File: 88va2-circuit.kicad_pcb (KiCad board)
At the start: 4 copper layers, 380 x 237.5 mm, 52 parts, among them CN2 FDD, CN4 TEXT BUS, CN5 LED, IC1 D65101GD055, IC13 SN74ALS374N, IC20 7407, IC21 uPD4990AC, IC22 DIP-14_W7.62mm, IC65 D65101GD110, IC8 SN74ALS374N, IC9 D65200GD076, X2 32.768K

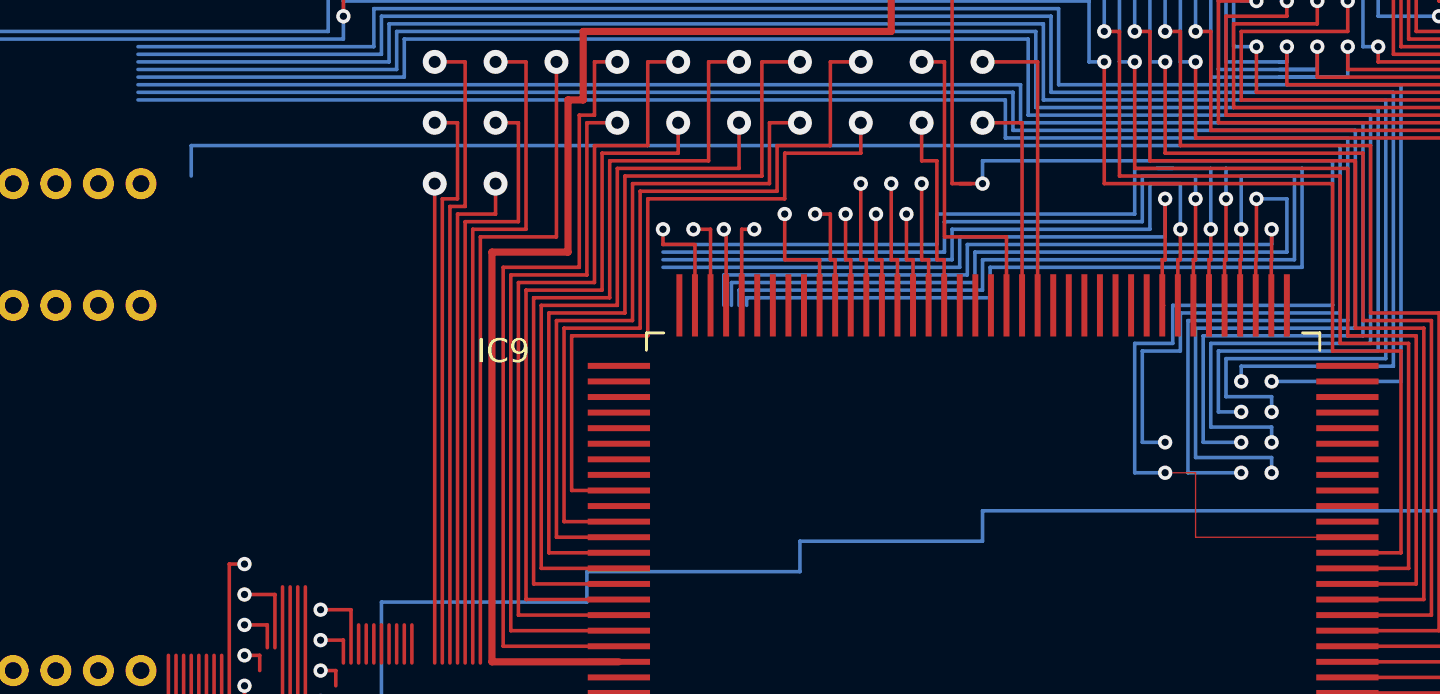
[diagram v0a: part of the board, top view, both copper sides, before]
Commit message: wiring IC9
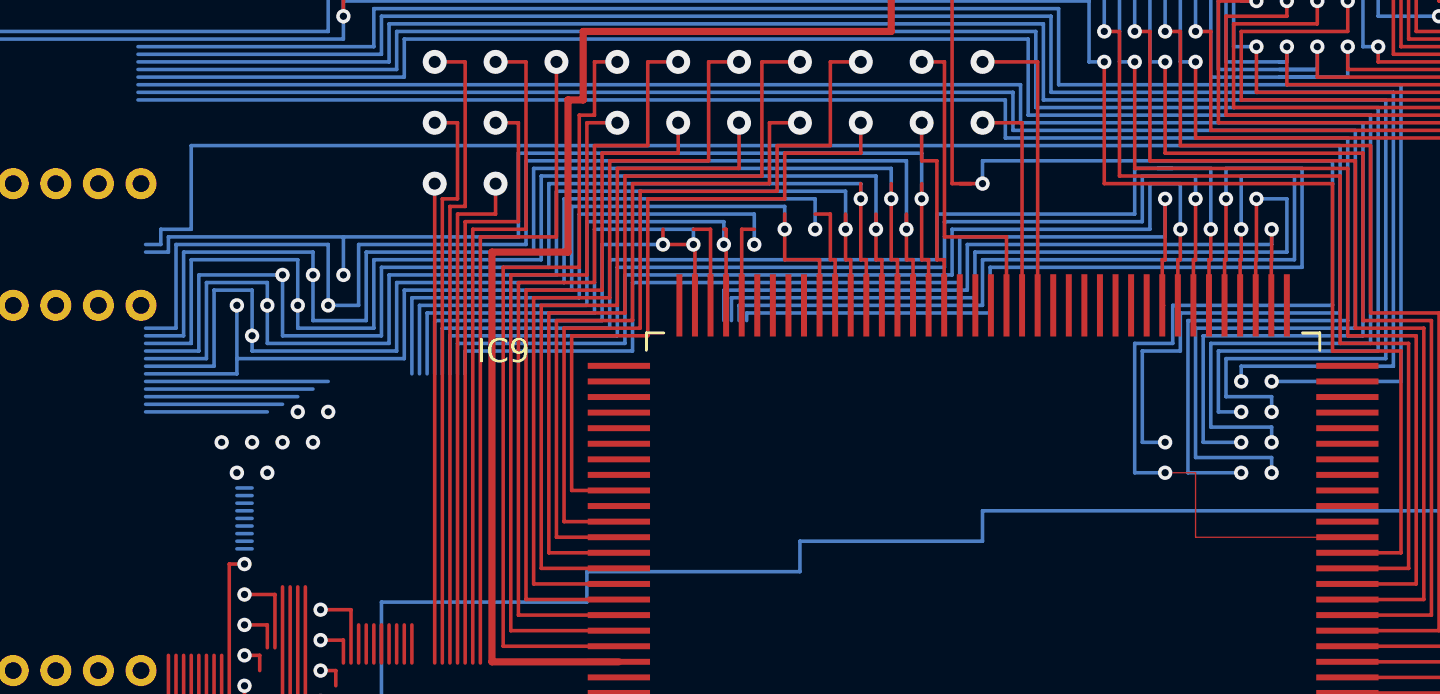
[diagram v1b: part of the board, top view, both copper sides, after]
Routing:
- net (no net): track 4000.6 -> 4515.6 mm, vias 74 -> 90
- net +5V: track 1140.2 -> 1144.0 mm

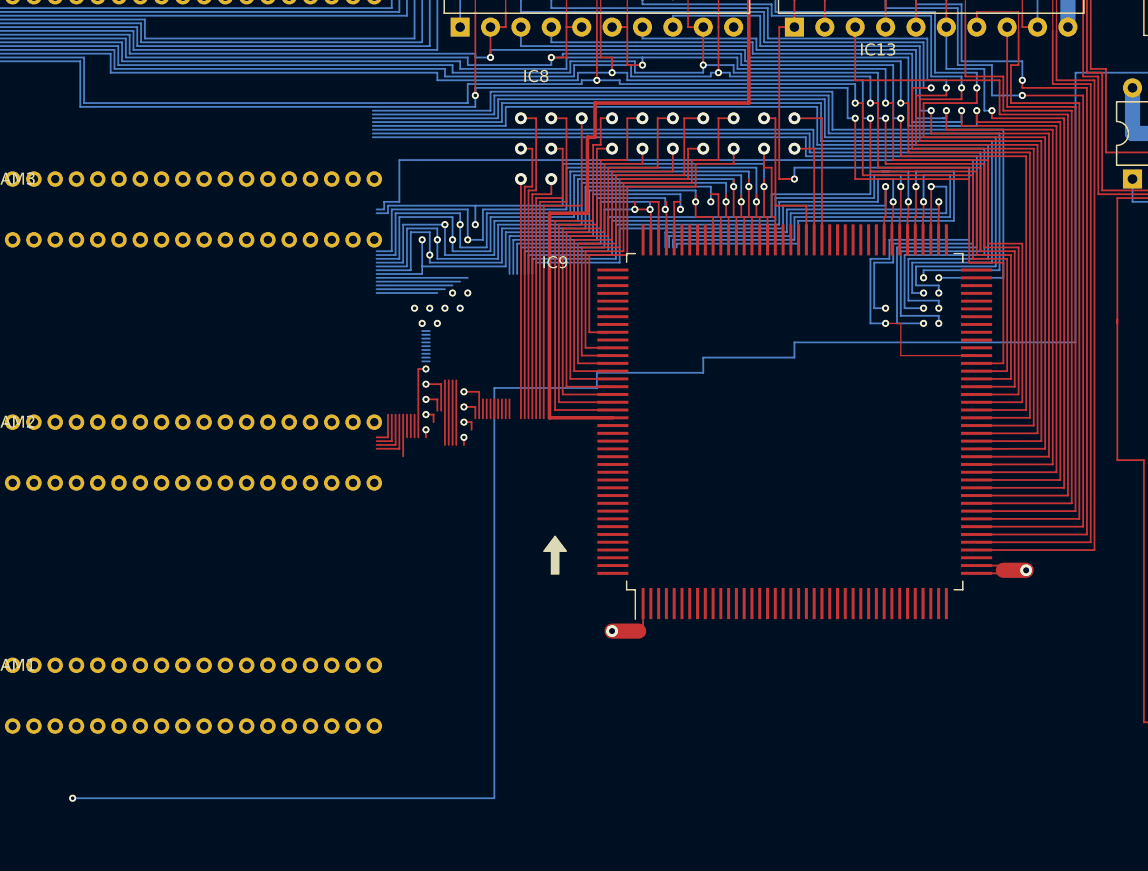
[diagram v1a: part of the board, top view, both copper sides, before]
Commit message: wiring IC9 and GVRAM
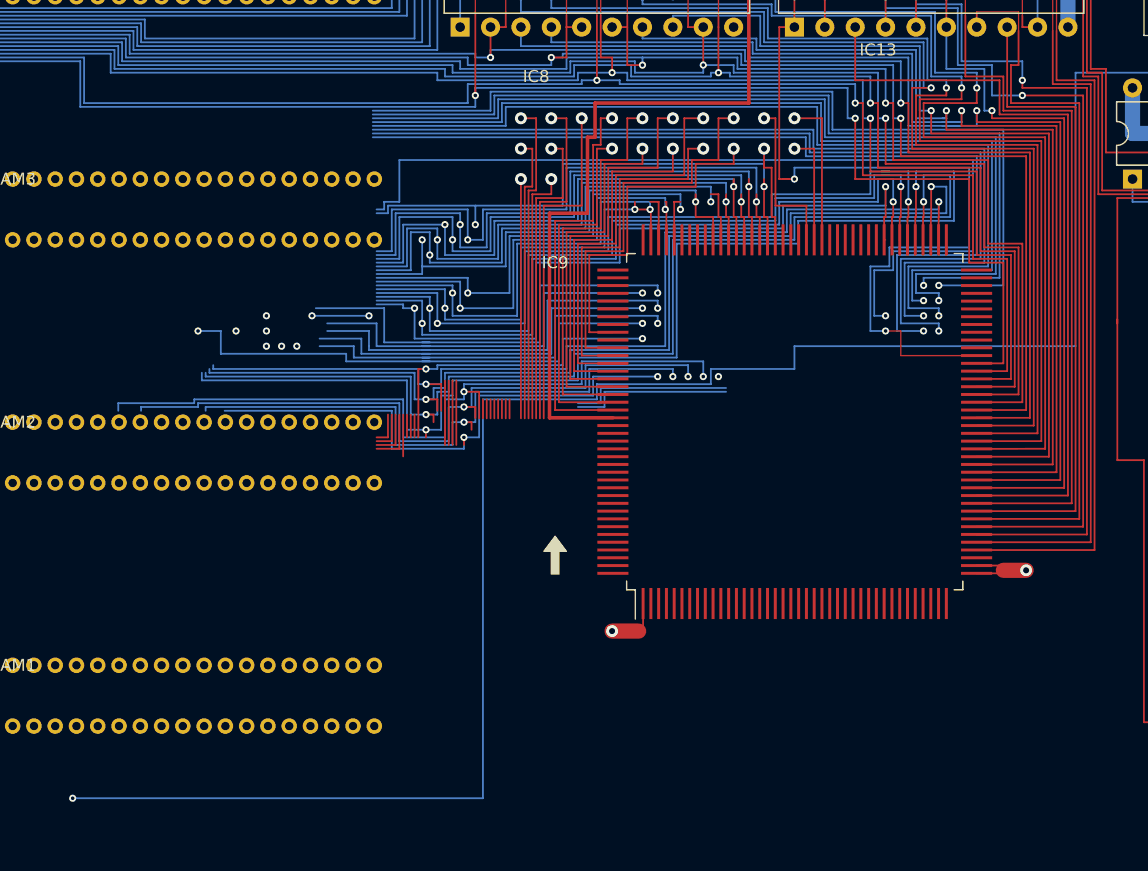
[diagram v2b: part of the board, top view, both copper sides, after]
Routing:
- net (no net): track 4515.6 -> 5333.8 mm, vias 90 -> 111

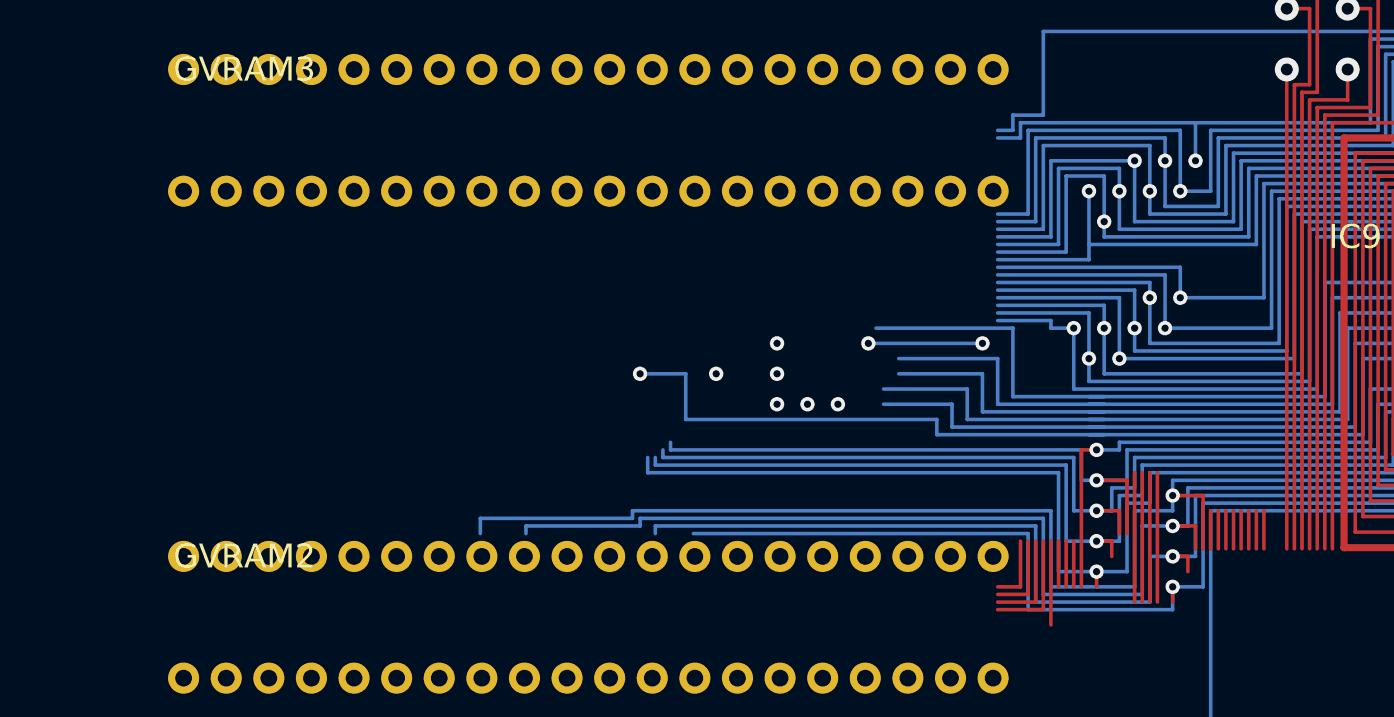
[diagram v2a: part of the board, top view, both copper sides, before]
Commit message: wiring IC9 and GVRAM
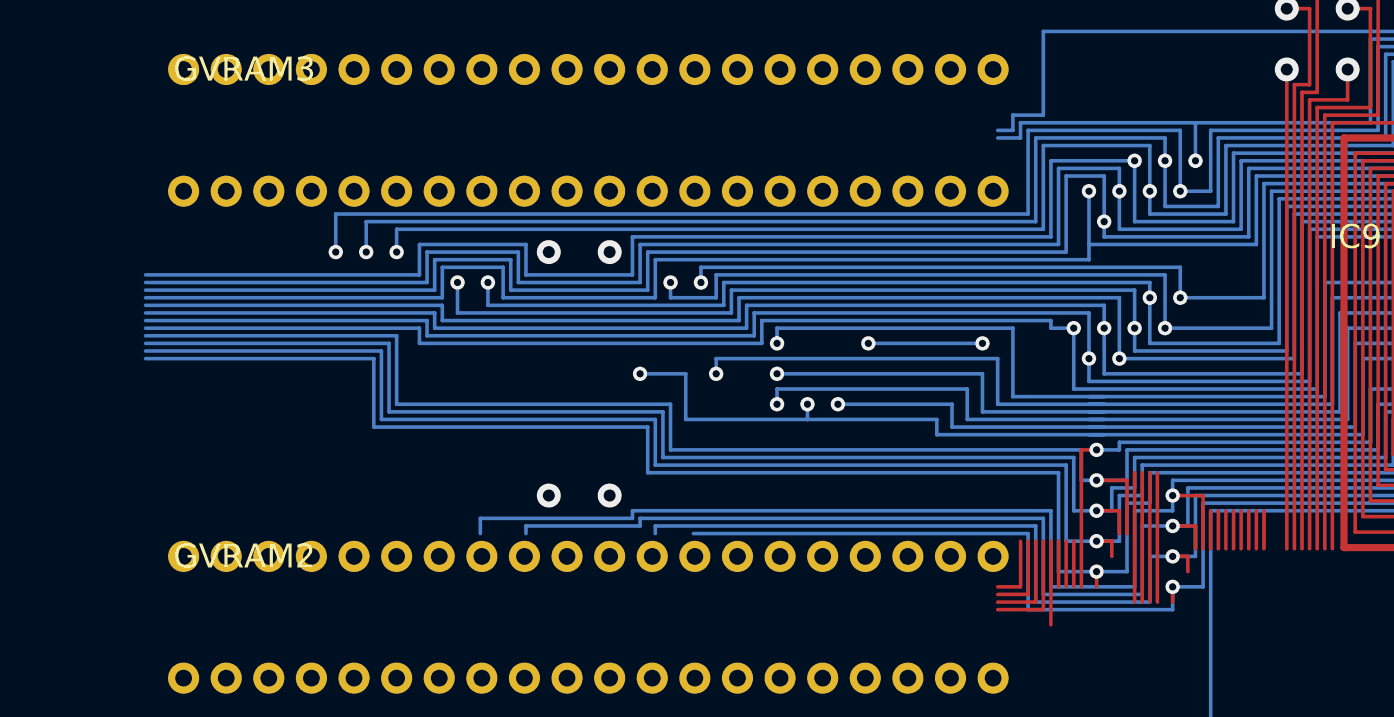
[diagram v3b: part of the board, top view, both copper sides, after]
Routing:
- net (no net): track 5333.8 -> 5929.1 mm, vias 111 -> 122

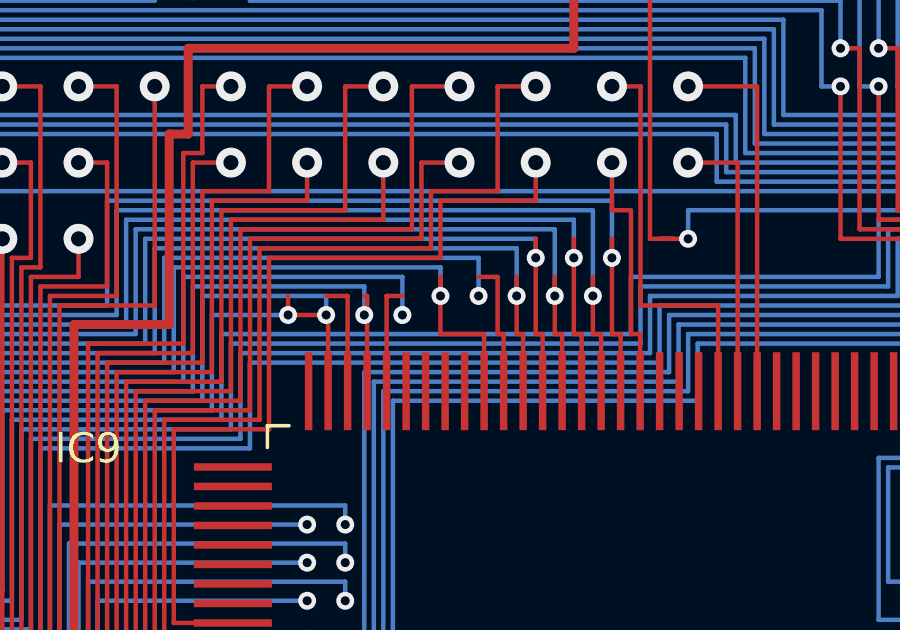
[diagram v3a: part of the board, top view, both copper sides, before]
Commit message: pcb: fix wire for IC9
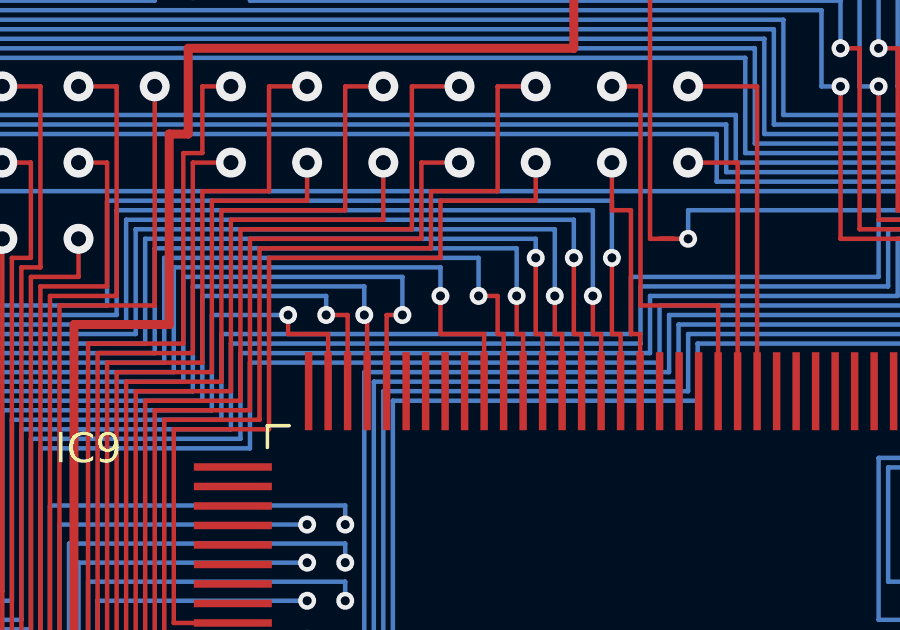
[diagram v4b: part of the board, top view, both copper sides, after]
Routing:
- net (no net): track 5929.1 -> 5921.5 mm
